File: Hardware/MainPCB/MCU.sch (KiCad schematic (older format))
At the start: 21 parts, among them J2 Conn_01x09_Female, J3 UART, U4 ESP32-WROOM-32D, U5 TPS22919, U6 TPS22919, U7 TPS22919

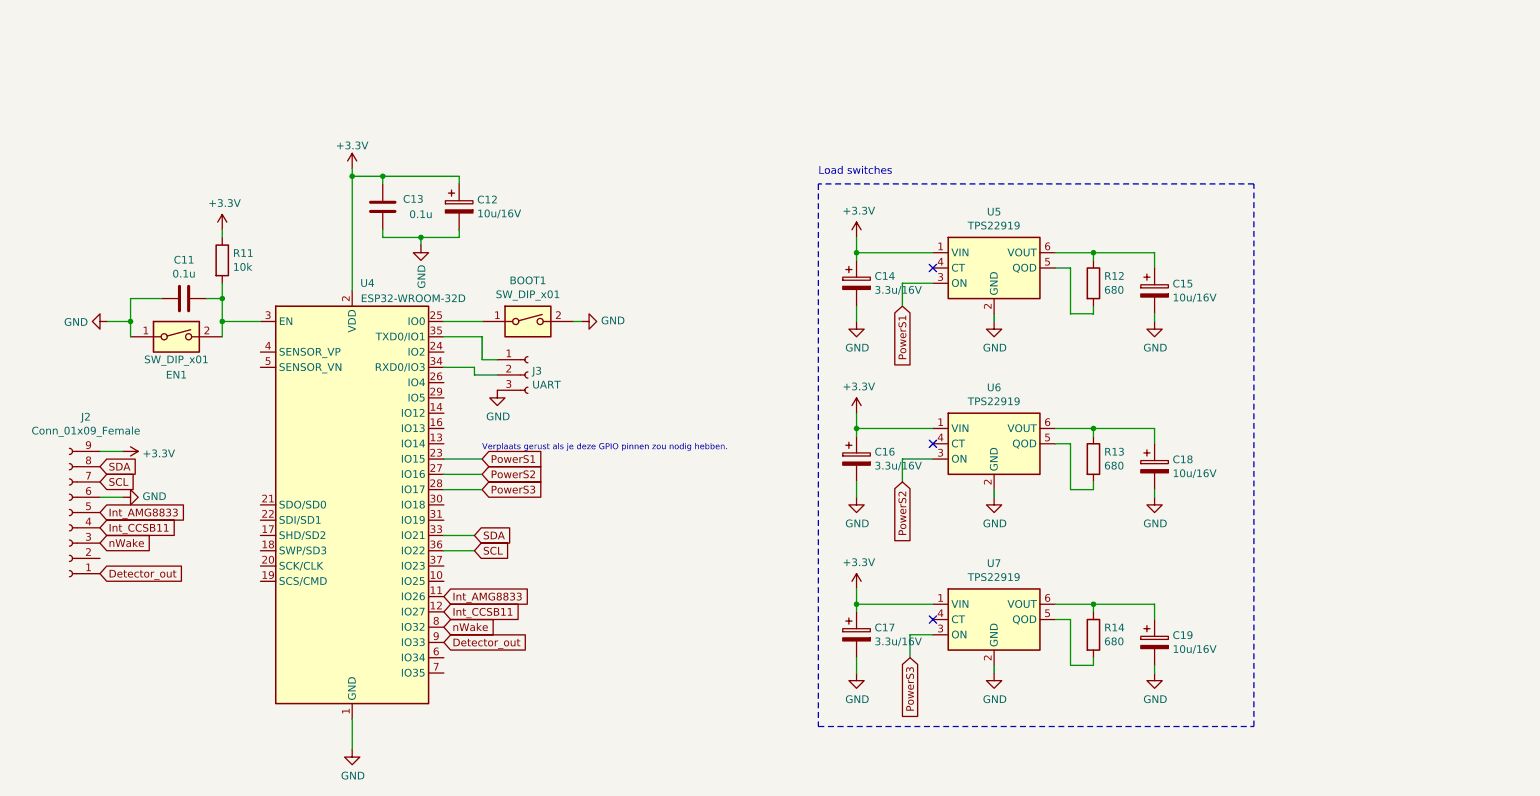
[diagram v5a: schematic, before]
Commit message: routed mcu part of main pcb
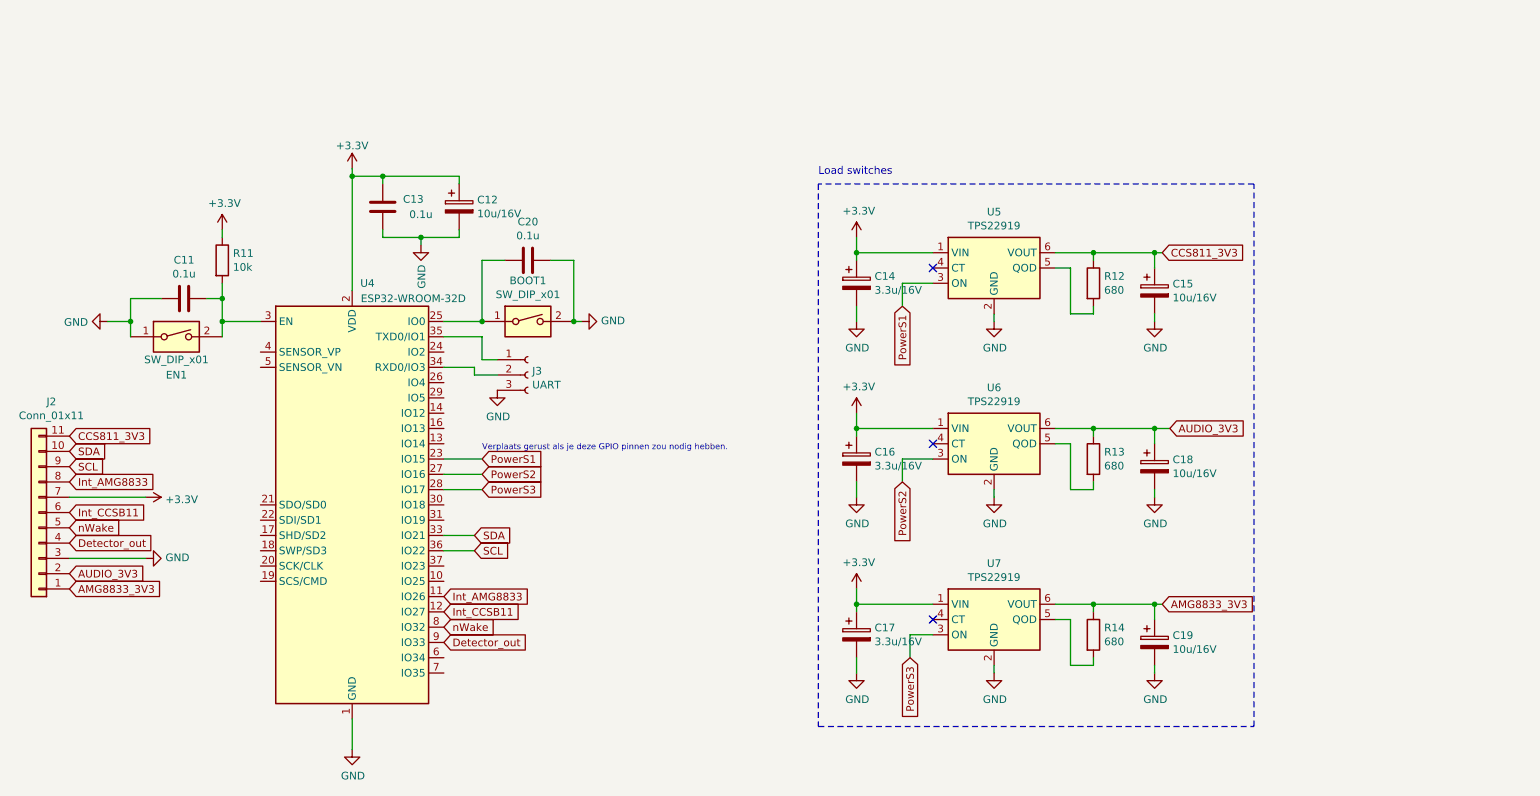
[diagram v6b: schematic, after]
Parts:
- removed J2: Conn_01x09_Female, Connector_PinHeader_2.54mm:PinHeader_1x09_P2.54mm_Vertical, symbol Connector:Conn_01x09_Female
- added C20: 0.1u, Capacitor_SMD:C_1206_3216Metric_Pad1.42x1.75mm_HandSolder, symbol Device:C
- added J2: Conn_01x11, Connector_PinHeader_2.54mm:PinHeader_1x11_P2.54mm_Vertical, symbol Connector_Generic:Conn_01x11
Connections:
- net +3V3: now also J2.7 (Pin_7)
- net Detector_out: now also J2.4 (Pin_4)
- net GND: now also C20.1, J2.3 (Pin_3)
- net Int_AMG8833: now also J2.8 (Pin_8)
- net Int_CCSB11: now also J2.6 (Pin_6)
- net SCL: now also J2.9 (Pin_9)
- net SDA: now also J2.10 (Pin_10)
- net nWake: now also J2.5 (Pin_5)
- net CCS811_3V3: now reaches C15.1, R12.1, U5.6 (VOUT)
- net CCS811_3V3: now also J2.11 (Pin_11)
- net at BOOT1.1, U4.25 (IO0): now also C20.2
- net AUDIO_3V3: now reaches C18.1, R13.1, U6.6 (VOUT)
- net AUDIO_3V3: now also J2.2 (Pin_2)
- net AMG8833_3V3: now reaches C19.1, R14.1, U7.6 (VOUT)
- net AMG8833_3V3: now also J2.1 (Pin_1)
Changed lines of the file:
@@
 Text GLabel 3800 4550 2    50   Input ~ 0
 SDA
-Text GLabel 1350 4100 2    50   Input ~ 0
+Text GLabel 1150 4000 2    50   Input ~ 0
 SDA
-Text GLabel 1350 4200 2    50   Input ~ 0
+Text GLabel 1150 4100 2    50   Input ~ 0
 SCL
 Wire Wire Line
@@
 L power:+3.3V #PWR030
 U 1 1 5E637941
-P 1500 4000
-F 0 "#PWR030" H 1500 3850 50  0001 C CNN
-F 1 "+3.3V" V 1515 4128 50  0000 L CNN
-F 2 "" H 1500 4000 50  0001 C CNN
-F 3 "" H 1500 4000 50  0001 C CNN
-	1    1500 4000
+P 1650 4300
+F 0 "#PWR030" H 1650 4150 50  0001 C CNN
+F 1 "+3.3V" V 1665 4428 50  0000 L CNN
+F 2 "" H 1650 4300 50  0001 C CNN
+F 3 "" H 1650 4300 50  0001 C CNN
+	1    1650 4300
 	0    1    1    0
 $EndComp
@@
 L power:GND #PWR031
 U 1 1 5E63843C
-P 1500 4300
-F 0 "#PWR031" H 1500 4050 50  0001 C CNN
-F 1 "GND" V 1505 4172 50  0000 R CNN
-F 2 "" H 1500 4300 50  0001 C CNN
-F 3 "" H 1500 4300 50  0001 C CNN
-	1    1500 4300
+P 1650 4700
+F 0 "#PWR031" H 1650 4450 50  0001 C CNN
+F 1 "GND" V 1655 4572 50  0000 R CNN
+F 2 "" H 1650 4700 50  0001 C CNN
+F 3 "" H 1650 4700 50  0001 C CNN
+	1    1650 4700
 	0    -1   -1   0
 $EndComp
-Wire Wire Line
-	1500 4000 1350 4000
-Wire Wire Line
-	1500 4300 1350 4300
-Text GLabel 1350 4400 2    50   Input ~ 0
+Text GLabel 1150 4200 2    50   Input ~ 0
 Int_AMG8833
-Text GLabel 1350 4500 2    50   Input ~ 0
+Text GLabel 1150 4400 2    50   Input ~ 0
 Int_CCSB11
-Text GLabel 1350 4600 2    50   Input ~ 0
+Text GLabel 1150 4500 2    50   Input ~ 0
 nWake
-Text GLabel 1350 4800 2    50   Input ~ 0
+Text GLabel 1150 4600 2    50   Input ~ 0
 Detector_out
-$Comp
-L Connector:Conn_01x09_Female J2
-U 1 1 5E62DF3B
-P 1150 4400
-F 0 "J2" H 1042 3775 50  0000 C CNN
-F 1 "Conn_01x09_Female" H 1042 3866 50  0000 C CNN
-F 2 "Connector_PinHeader_2.54mm:PinHeader_1x09_P2.54mm_Vertical" H 1150 4400 50  0001 C CNN
-F 3 "~" H 1150 4400 50  0001 C CNN
-	1    1150 4400
-	-1   0    0    1
-$EndComp
 Text GLabel 3600 4950 2    50   Input ~ 0
 Int_AMG8833
@@
 Wire Wire Line
 	6650 5200 6800 5200
+$Comp
+L Connector_Generic:Conn_01x11 J2
+U 1 1 5E6AB884
+P 950 4400
+F 0 "J2" H 868 3675 50  0000 C CNN
+F 1 "Conn_01x11" H 868 3766 50  0000 C CNN
+F 2 "Connector_PinHeader_2.54mm:PinHeader_1x11_P2.54mm_Vertical" H 950 4400 50  0001 C CNN
+F 3 "~" H 950 4400 50  0001 C CNN
+	1    950  4400
+	-1   0    0    1
+$EndComp
+Wire Wire Line
+	1650 4700 1150 4700
+Wire Wire Line
+	1150 4300 1650 4300
+Text GLabel 1150 4800 2    50   Input ~ 0
+AUDIO_3V3
+Text GLabel 1150 4900 2    50   Input ~ 0
+AMG8833_3V3
+Text GLabel 1150 3900 2    50   Input ~ 0
+CCS811_3V3
+Text GLabel 8300 2700 2    50   Input ~ 0
+CCS811_3V3
+Text GLabel 8350 3850 2    50   Input ~ 0
+AUDIO_3V3
+Text GLabel 8300 5000 2    50   Input ~ 0
+AMG8833_3V3
+Wire Wire Line
+	8300 5000 8250 5000
+Connection ~ 8250 5000
+Wire Wire Line
+	8250 3850 8350 3850
+Connection ~ 8250 3850
+Wire Wire Line
+	8250 2700 8300 2700
+Connection ~ 8250 2700
+$Comp
+L Device:C C20
+U 1 1 5E6CAA64
+P 4150 2750
+F 0 "C20" V 3898 2750 50  0000 C CNN
+F 1 "0.1u" V 3989 2750 50  0000 C CNN
+F 2 "Capacitor_SMD:C_1206_3216Metric_Pad1.42x1.75mm_HandSolder" H 4188 2600 50  0001 C CNN
+F 3 "~" H 4150 2750 50  0001 C CNN
+	1    4150 2750
+	0    1    1    0
+$EndComp
+Wire Wire Line
+	4450 3150 4450 2750
+Wire Wire Line
+	4450 2750 4300 2750
+Connection ~ 4450 3150
+Wire Wire Line
+	4000 2750 3850 2750
+Wire Wire Line
+	3850 2750 3850 3150
+Connection ~ 3850 3150
 $EndSCHEMATC

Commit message: Finished MainPCB + generated gerber files + aanpassingen BOM
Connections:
- net Detector_out: now also J2.5 (Pin_5); no longer J2.4 (Pin_4)
- net Int_CCSB11: now also J2.4 (Pin_4); no longer J2.6 (Pin_6)
- net SCL: now also J2.10 (Pin_10); no longer J2.9 (Pin_9)
- net SDA: now also J2.9 (Pin_9); no longer J2.10 (Pin_10)
- net nWake: now also J2.6 (Pin_6); no longer J2.5 (Pin_5)
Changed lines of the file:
@@
 Text GLabel 3800 4550 2    50   Input ~ 0
 SDA
+Text GLabel 1150 4100 2    50   Input ~ 0
+SDA
 Text GLabel 1150 4000 2    50   Input ~ 0
-SDA
-Text GLabel 1150 4100 2    50   Input ~ 0
 SCL
 Wire Wire Line
@@
 Text GLabel 1150 4200 2    50   Input ~ 0
 Int_AMG8833
+Text GLabel 1150 4600 2    50   Input ~ 0
+Int_CCSB11
 Text GLabel 1150 4400 2    50   Input ~ 0
-Int_CCSB11
+nWake
 Text GLabel 1150 4500 2    50   Input ~ 0
-nWake
-Text GLabel 1150 4600 2    50   Input ~ 0
 Detector_out
 Text GLabel 3600 4950 2    50   Input ~ 0
